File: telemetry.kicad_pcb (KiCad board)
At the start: 2 copper layers, 176.3 x 79.5 mm, 63 parts, among them J1 DT13-08PA, J10 DT13-4P, J11 Conn_01x03, J12 Conn_01x03, J13 Conn_01x03, J14 Conn_01x03, J2 DT13-6P, J3 Conn_01x06, J4 Conn_01x06, J5 Conn_01x06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

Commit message: added ESP32, connector footprint
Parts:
- removed L2: 12u, Inductor_SMD:L_6.3x6.3_H3
- removed R19, R22, R23, R24: 0, Jumper:SolderJumper-2_P1.3mm_Open_TrianglePad1.0x1.5mm
- removed R21: 100, Resistor_SMD:R_0805_2012Metric
- removed U1: ~, Telemetry:ESP32_30pin
- removed U7: R-78E3.3-0.5, Converter_DCDC:Converter_DCDC_RECOM_R-78E-0.5_THT
- added C13: 10n, Capacitor_SMD:C_0805_2012Metric, F.Cu at (150.2, 175.0)
- added C14: 10n, Capacitor_SMD:C_0805_2012Metric, F.Cu at (150.2, 178.0)
- added C8: 10n, Capacitor_SMD:C_0805_2012Metric, F.Cu at (150.2, 165.9)
- added C9: 10n, Capacitor_SMD:C_0805_2012Metric, F.Cu at (150.2, 168.9)
- added D3: SS34, Diode_SMD:D_SMA, F.Cu at (161.0, 166.7)
- added D4: SMBJ24CA, Diode_SMD:D_SMB, F.Cu at (162.1, 192.4)
- added F1: MF-USHT075KX/24-2, Inductor_SMD:L_1210_3225Metric, F.Cu at (159.7, 171.1)
- added J15: Conn_01x03, Connector_JST:JST_XA_B03B-XASK-1_1x03_P2.50mm_Vertical, F.Cu at (139.5, 160.2)
- added J16: Conn_01x03, Connector_JST:JST_XA_B03B-XASK-1_1x03_P2.50mm_Vertical, F.Cu at (139.5, 168.7)
- added J17: Conn_01x03, Connector_JST:JST_XA_B03B-XASK-1_1x03_P2.50mm_Vertical, F.Cu at (139.5, 177.1)
- added J18: Conn_01x03, Connector_JST:JST_XA_B03B-XASK-1_1x03_P2.50mm_Vertical, F.Cu at (139.5, 185.6)
- added J19: Conn_01x03, Connector_JST:JST_XA_B03B-XASK-1_1x03_P2.50mm_Vertical, F.Cu at (139.5, 194.0)
- added U2: Waveshare ESP32-S3 Devboard, Connector_PinSocket_2.54mm:PinSocket_1x22_P2.54mm_Vertical, F.Cu at (238.8, -1.13)
- added U3: TLV76133DCY, Package_TO_SOT_SMD:SOT-223-3_TabPin2, F.Cu at (152.9, 193.8)
- C1: value 4.7u -> 1u
- C2: value 4.7u -> 10u
- C3: value 10u -> 2.2u
- J10: value DT13-4P -> Conn_01x02; footprint Connector_DT:TE_DT13-4P -> Connector_DT:TE_DT13-2P
- J14: value Conn_01x03 -> Conn_01x06; footprint Connector_JST:JST_XA_B03B-XASK-1_1x03_P2.50mm_Vertical -> Connector_JST:JST_XA_B06B-XASK-1_1x06_P2.50mm_Vertical
- J2: value DT13-6P -> Conn_01x02; footprint Connector_DT:TE_DT13-6P -> Connector_DT:TE_DT13-2P
- R13: value 0 -> 100; footprint Jumper:SolderJumper-2_P1.3mm_Open_TrianglePad1.0x1.5mm -> Resistor_SMD:R_0805_2012Metric
- U5: value R-78E5.0-0.5 -> R-78C5.0-1.0
- moved C3 134.4 mm to (200.0, 21.9)
- moved R13 117.9 mm to (154.7, 177.7)
- moved C12 113.1 mm to (150.2, 171.9), turned to 0 degrees
- moved R12 100.5 mm to (154.7, 174.8), turned to 0 degrees
- moved J14 98.7 mm to (151.6, 160.2), turned to 0 degrees
- moved U5 95.8 mm to (152.2, 186.8), turned to 0 degrees
- moved R6 86.2 mm to (154.7, 165.9), turned to 0 degrees
- moved C1 78.0 mm to (200.0, 18.8), turned to 0 degrees
- moved R10 77.2 mm to (154.7, 168.8), turned to 0 degrees
- moved R11 69.2 mm to (154.7, 171.8), turned to 0 degrees
- moved J10 22.1 mm to (171.3, 62.1)
- moved J2 13.1 mm to (133.0, 61.6)
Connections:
- C1 pad 1: Net-(U7-IN) -> +5V
- C12 pad 1: /A3 -> /A5
- C3 pad 1: +12V -> +3V3
- C4 pad 1: +12V -> /PSU+
- J1 pad 1: /A0_SIG -> /W0
- J1 pad 2: /A1_SIG -> /W1
- J1 pad 3: /A2_SIG -> /W2
- J1 pad 4: /A3_SIG -> /W3
- J10 pad 1: +12V -> /CANH
- J10 pad 2: /CANH -> /CANL
- J11 pad 2: Net-(J11-Pin_2) -> /A6_SIG
- J12 pad 2: Net-(J12-Pin_2) -> /A7_SIG
- J13 pad 2: Net-(J13-Pin_2) -> /A5_SIG
- J14 pad 1: +3V3 -> +5V
- J14 pad 2: Net-(J14-Pin_2) -> /I2C1_1_GPIO
- J14 pad 3: GND -> /GPS(SCL/RX)
- J2 pad 1: +3V3 -> +12V
- J2 pad 2: /GPS0 -> GND
- L1 pad 1: +12V -> /PSU+
- R10 pad 1: Net-(J11-Pin_2) -> /A4
- R10 pad 2: /D1 -> /A4_SIG
- R11 pad 1: Net-(J12-Pin_2) -> /A5
- R11 pad 2: /D2 -> /A5_SIG
- R12 pad 1: Net-(J14-Pin_2) -> /A6
- R12 pad 2: /D3 -> /A6_SIG
- R13 pad 1: /I2C0_SDA -> /A7
- R13 pad 2: /GPS1 -> /A7_SIG
- R6 pad 1: Net-(J13-Pin_2) -> /A3
- R6 pad 2: /D0 -> /A3_SIG
- U6 pad 1: /CANTX -> /CAN_TX
- U6 pad 4: /CANRX -> /CAN_RX
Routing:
- net (no net): track 0.00 -> 230.6 mm
- net /D3: track 76.3 -> 0.00 mm
- net /D0: track 60.3 -> 0.00 mm
- net /D1: track 49.4 -> 0.00 mm
- net /D2: track 38.5 -> 0.00 mm
- net /PSU+: track 0.00 -> 36.0 mm
- net +12V: track 36.0 -> 0.00 mm
- net Net-(J14-Pin_2): track 6.19 -> 0.00 mm
- net Net-(J13-Pin_2): track 6.17 -> 0.00 mm
- net /A5_SIG: track 0.00 -> 6.17 mm
- net Net-(J11-Pin_2): track 6.15 -> 0.00 mm
- net /A6_SIG: track 0.00 -> 6.15 mm
- net Net-(J12-Pin_2): track 6.13 -> 0.00 mm
- net /A7_SIG: track 0.00 -> 6.13 mm
- net /W3: track 0.00 -> 5.91 mm
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
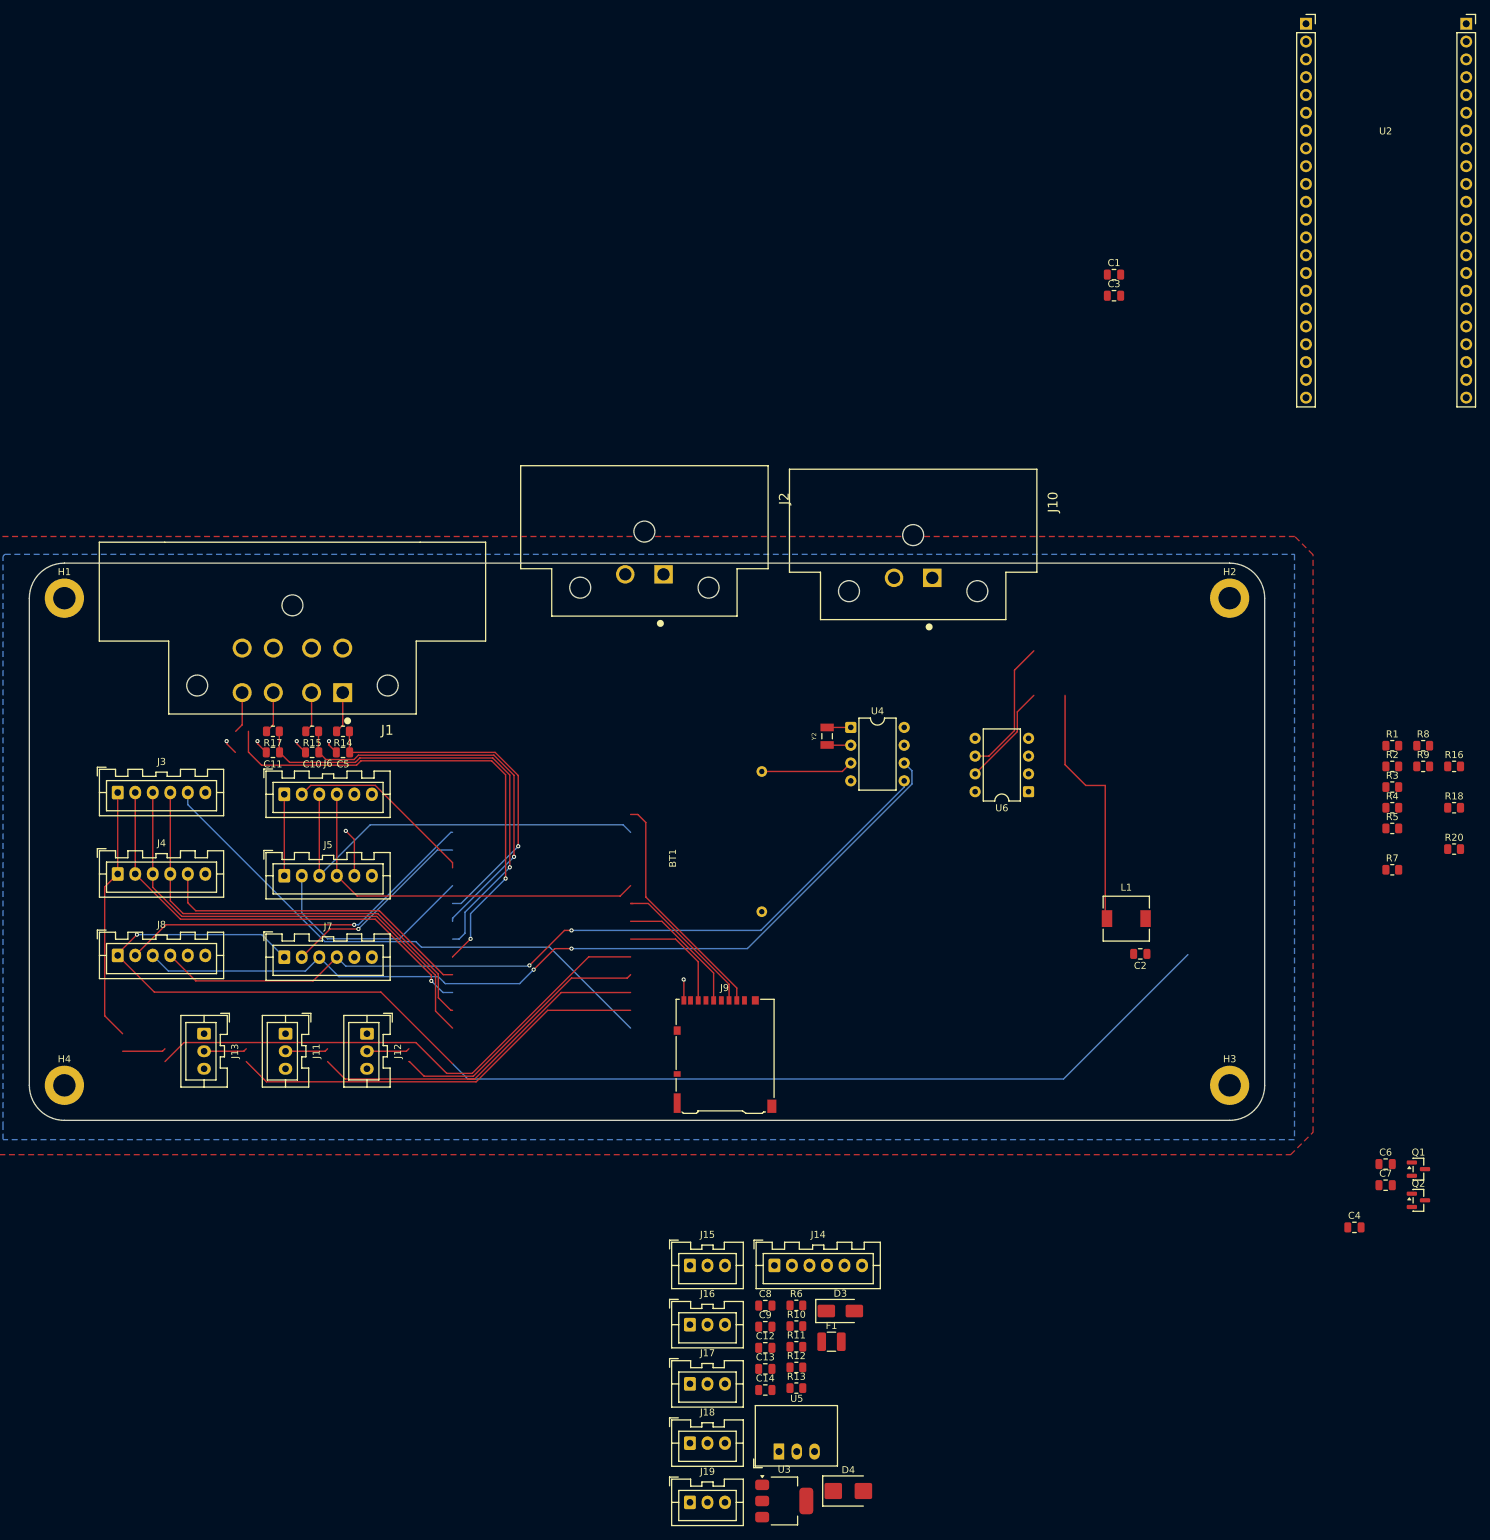
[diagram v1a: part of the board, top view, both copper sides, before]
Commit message: Place and route important components
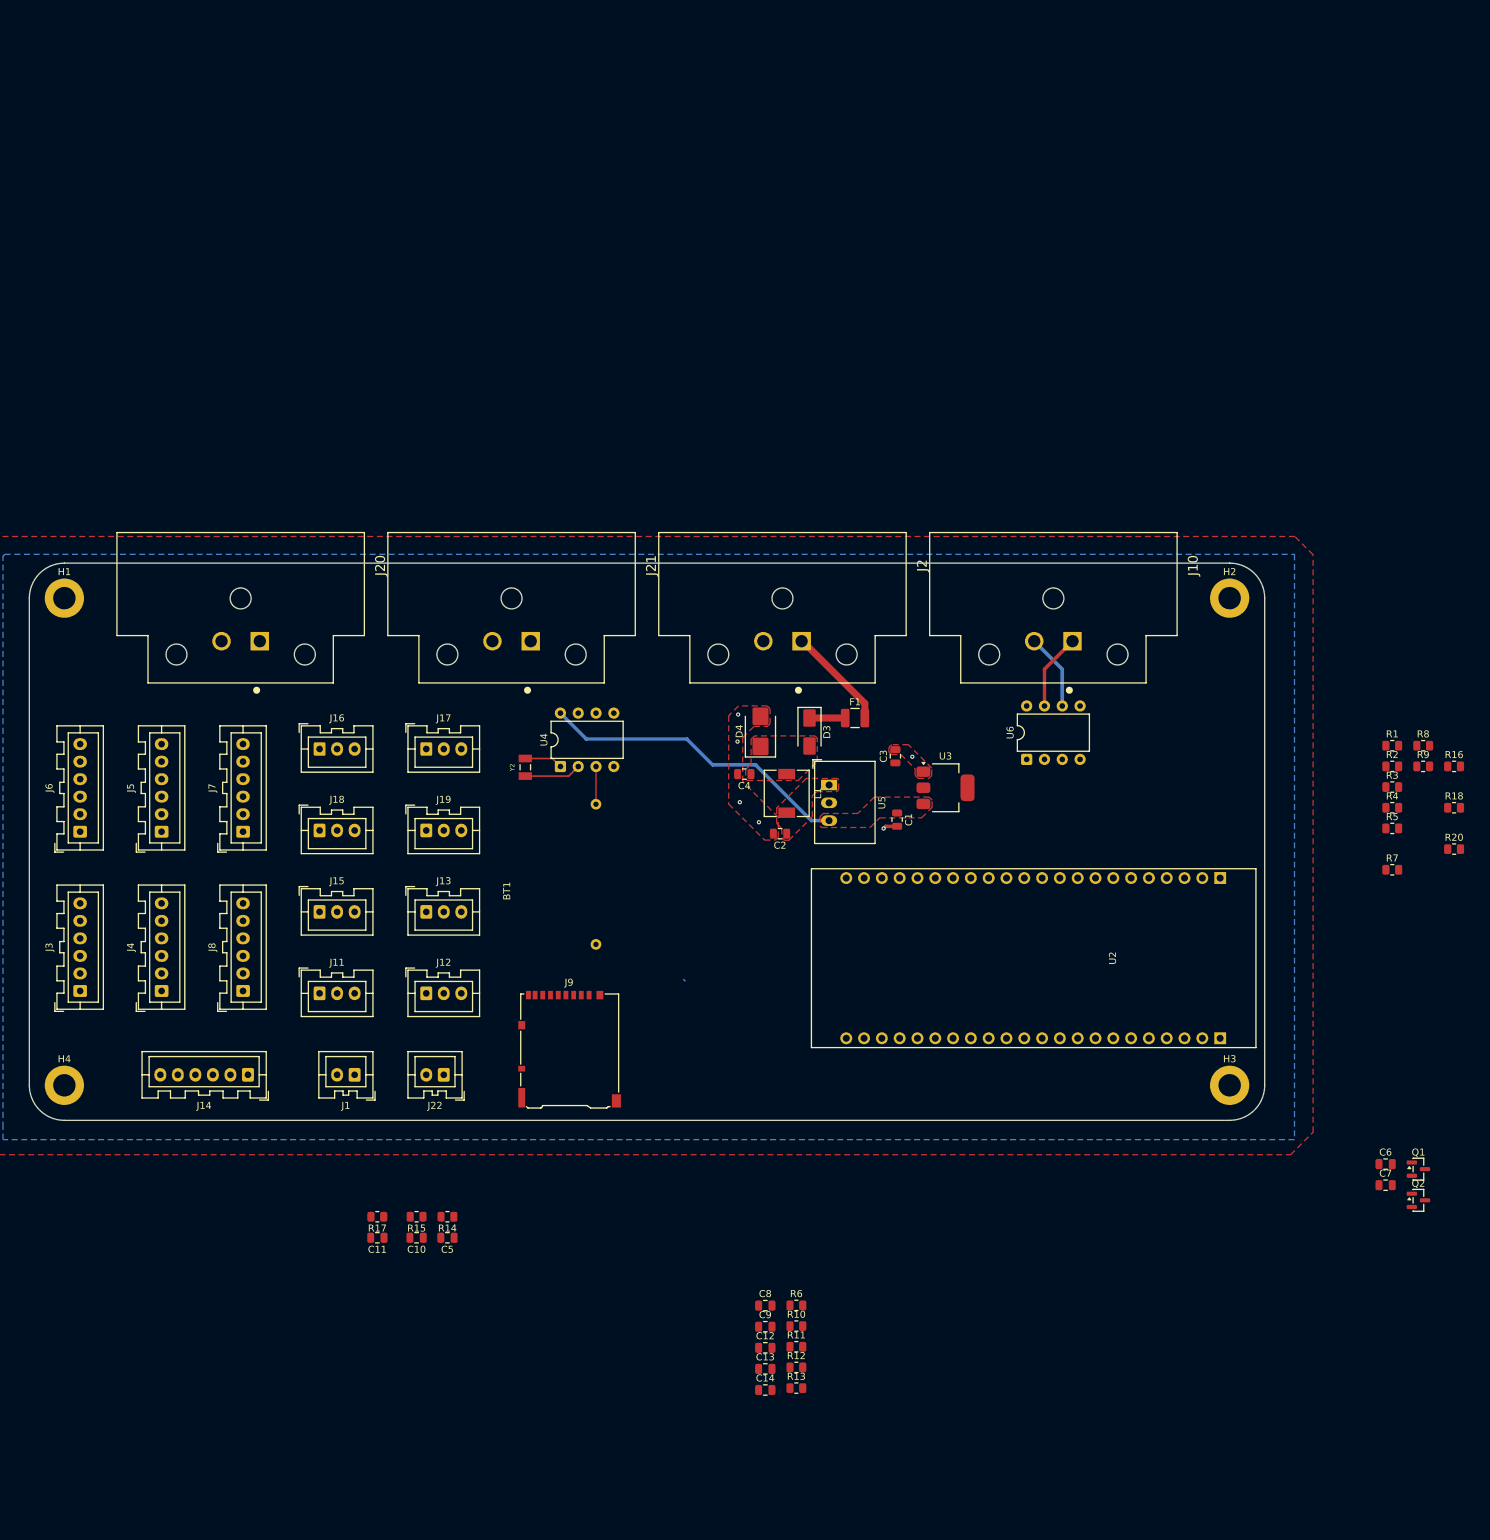
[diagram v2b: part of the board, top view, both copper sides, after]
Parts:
- added J20: DT13-2P, Connector_DT:TE_DT13-2P, F.Cu at (75.4, 71.1)
- added J21: DT13-2P, Connector_DT:TE_DT13-2P, F.Cu at (114.0, 71.1)
- added J22: Conn_01x02, Connector_JST:JST_XA_B02B-XASK-1_1x02_P2.50mm_Vertical, F.Cu at (104.4, 133.0)
- J1: value DT13-08PA -> Conn_01x02; footprint Connector_DT:TE_DT13-08PA -> Connector_JST:JST_XA_B02B-XASK-1_1x02_P2.50mm_Vertical
- J10, J2: value Conn_01x02 -> DT13-2P
- moved U2 123.9 mm to (199.3, 116.4), turned to -90 degrees
- moved D4 109.1 mm to (149.6, 84.0), turned to 90 degrees
- moved C4 108.4 mm to (147.3, 90.1), turned to 180 degrees
- moved U3 104.3 mm to (176.0, 92.0)
- moved J19 103.0 mm to (101.9, 98.1)
- moved J18 102.1 mm to (86.7, 98.1)
- moved J17 98.1 mm to (101.9, 86.5)
- moved J16 97.7 mm to (86.7, 86.5)
- moved U5 95.4 mm to (159.3, 91.7), turned to -90 degrees
- moved F1 89.0 mm to (163.1, 82.1)
- moved C1 83.7 mm to (169.1, 96.6), turned to -90 degrees
- moved D3 82.7 mm to (156.6, 84.1), turned to -90 degrees
- moved J14 79.9 mm to (76.4, 133.0), turned to 180 degrees
- moved J15 73.0 mm to (86.7, 109.8)
- moved C3 72.7 mm to (168.8, 87.5), turned to 90 degrees
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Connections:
- J1 pad 2: /W1 -> GND
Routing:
- net (no net): track 230.6 -> 0.00 mm
- net +5V: track 193.9 -> 44.7 mm, vias 1 -> 0
- net /I2C1_SCL: track 126.9 -> 0.00 mm, vias 2 -> 0
- net /I2C1_SDA: track 119.6 -> 0.00 mm, vias 2 -> 0
- net /SPI1_0_CS: track 78.1 -> 0.00 mm
- net /A3: track 70.6 -> 0.00 mm, vias 2 -> 0
- net /SPI1_MOSI: track 67.6 -> 0.00 mm
- net /A2: track 65.1 -> 0.00 mm, vias 1 -> 0
- net /SPI1_SCK: track 64.4 -> 0.00 mm, vias 1 -> 0
- net /SPI1_MISO: track 64.2 -> 0.00 mm
- net /I2C0_SCL: track 59.5 -> 0.00 mm
- net /A1: track 57.2 -> 0.00 mm, vias 1 -> 0
- net /I2C0_SDA: track 55.3 -> 0.00 mm
- net /I2C1_1_GPIO: track 52.6 -> 0.00 mm, vias 1 -> 0
- net /A0: track 51.3 -> 0.00 mm, vias 1 -> 0
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- added copper zone on F.Cu, net +5V
- added copper zone on F.Cu, net /PSU+
- added copper zone on F.Cu, net GND
- added copper zone on F.Cu, net Net-(U5-IN)

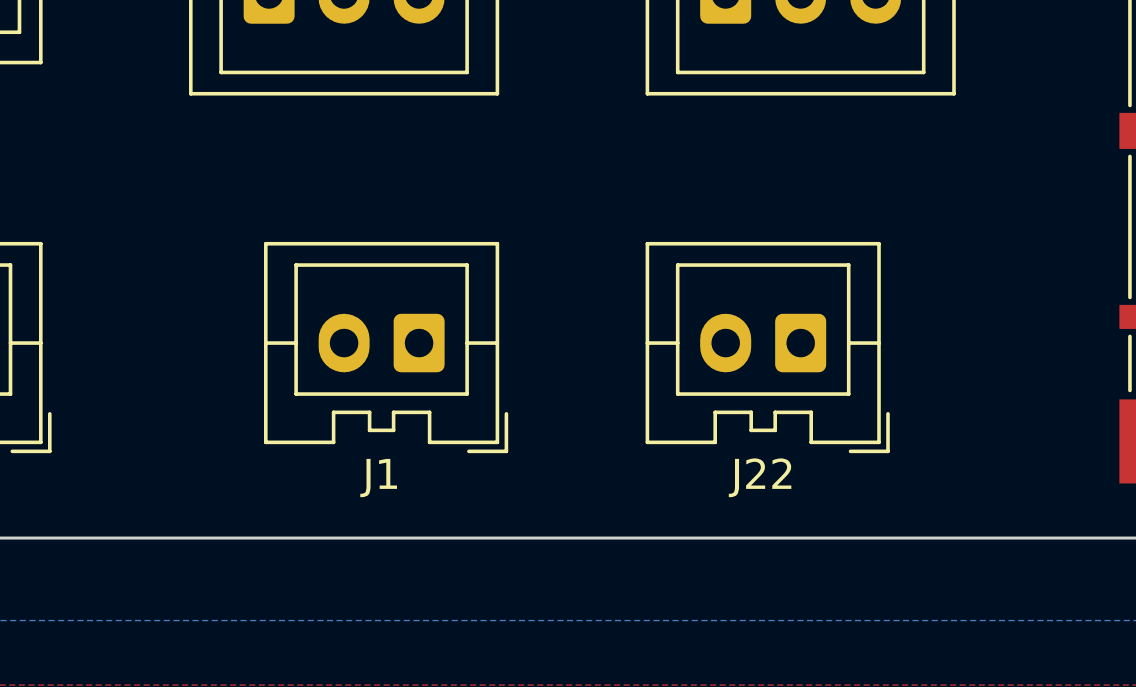
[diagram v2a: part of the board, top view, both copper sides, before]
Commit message: Add +3V3 pin to internal WSS connectors
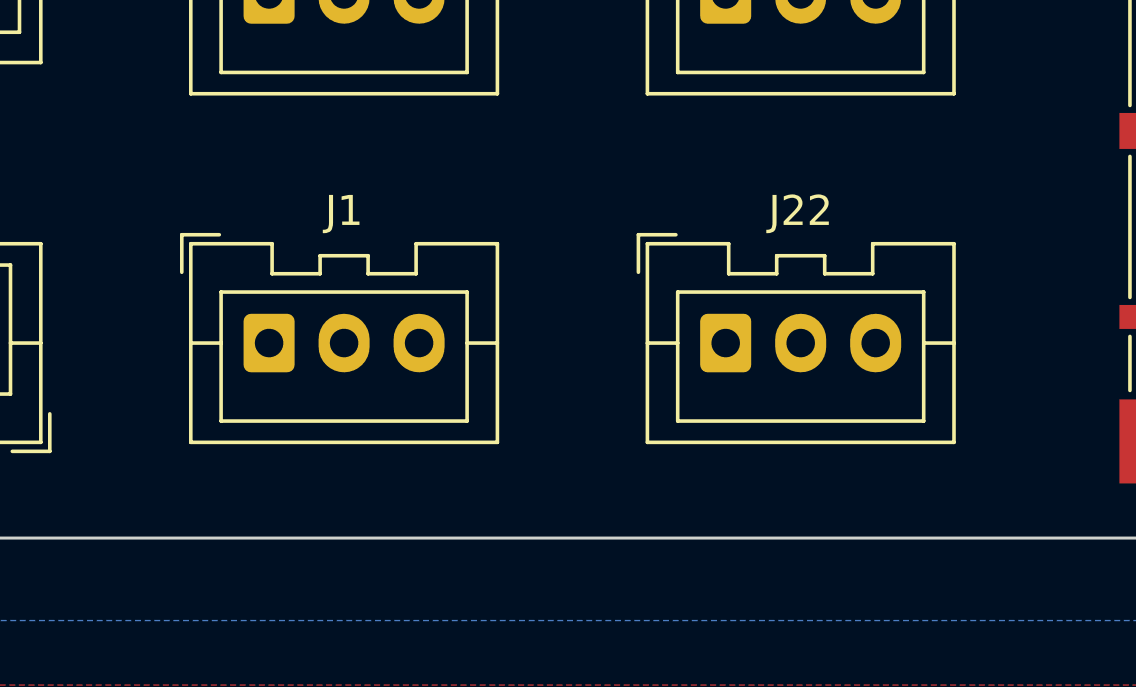
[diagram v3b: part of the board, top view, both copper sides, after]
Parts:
- J1, J22: value Conn_01x02 -> Conn_01x03; footprint Connector_JST:JST_XA_B02B-XASK-1_1x02_P2.50mm_Vertical -> Connector_JST:JST_XA_B03B-XASK-1_1x03_P2.50mm_Vertical
- moved J1 5.00 mm to (86.7, 133.0), turned to 0 degrees
- moved J22 2.50 mm to (101.9, 133.0), turned to 0 degrees
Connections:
- J1 pad 1: /W0 -> +3V3
- J1 pad 2: GND -> /W0
- J22 pad 1: /W1 -> +3V3
- J22 pad 2: GND -> /W1
- U2 pad 23: (no net) -> GND
- U2 pad 24: (no net) -> unconnected-(U2-GPIO43-Pad24)
- U2 pad 25: (no net) -> unconnected-(U2-GPIO44-Pad25)
- U2 pad 26: (no net) -> /W2
- U2 pad 27: (no net) -> /I2C0_SCL
- U2 pad 28: (no net) -> /GPS(SCL/RX)
- U2 pad 29: (no net) -> /GPS(SDA/TX)
- U2 pad 30: (no net) -> /SPI1_MISO
- U2 pad 31: (no net) -> /SPI1_SCK
- U2 pad 32: (no net) -> /SPI1_0_CS
- U2 pad 33: (no net) -> /SPI1_MOSI
- U2 pad 34: (no net) -> unconnected-(U2-GPIO36-Pad34)
- U2 pad 35: (no net) -> /I2C0_SDA
- U2 pad 36: (no net) -> /I2C1_1_GPIO
- U2 pad 37: (no net) -> /I2C1_0_GPIO
- U2 pad 38: (no net) -> /W3
- U2 pad 39: (no net) -> /W1
- U2 pad 40: (no net) -> /W0
- U2 pad 41: (no net) -> unconnected-(U2-GPIO20-Pad41)
- U2 pad 42: (no net) -> unconnected-(U2-GPIO19-Pad42)
- U2 pad 43: (no net) -> GND
- U2 pad 44: (no net) -> GND

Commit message: Switch to SIG+3V3 for Back WSS
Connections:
- J20 pad 1: /W2 -> +3V3
- J20 pad 2: GND -> /W2
- J21 pad 1: /W3 -> +3V3
- J21 pad 2: GND -> /W3
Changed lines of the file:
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@@
 			(layers "*.Cu" "*.Mask")
 			(remove_unused_layers no)
-			(net 29 "/W2")
+			(net 5 "+3V3")
 			(pinfunction "Pin_1")
 			(pintype "passive")
@@
 			(layers "*.Cu" "*.Mask")
 			(remove_unused_layers no)
-			(net 2 "GND")
+			(net 29 "/W2")
 			(pinfunction "Pin_2")
 			(pintype "passive")
@@
 			(layers "*.Cu" "*.Mask")
 			(remove_unused_layers no)
-			(net 27 "/W3")
+			(net 5 "+3V3")
 			(pinfunction "Pin_1")
 			(pintype "passive")
@@
 			(layers "*.Cu" "*.Mask")
 			(remove_unused_layers no)
-			(net 2 "GND")
+			(net 27 "/W3")
 			(pinfunction "Pin_2")
 			(pintype "passive")
